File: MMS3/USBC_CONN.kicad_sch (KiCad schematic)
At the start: 7 parts, among them J800 USB_C_Receptacle_USB2.0_16P, U401 TPD2EUSB30DRTR-TP

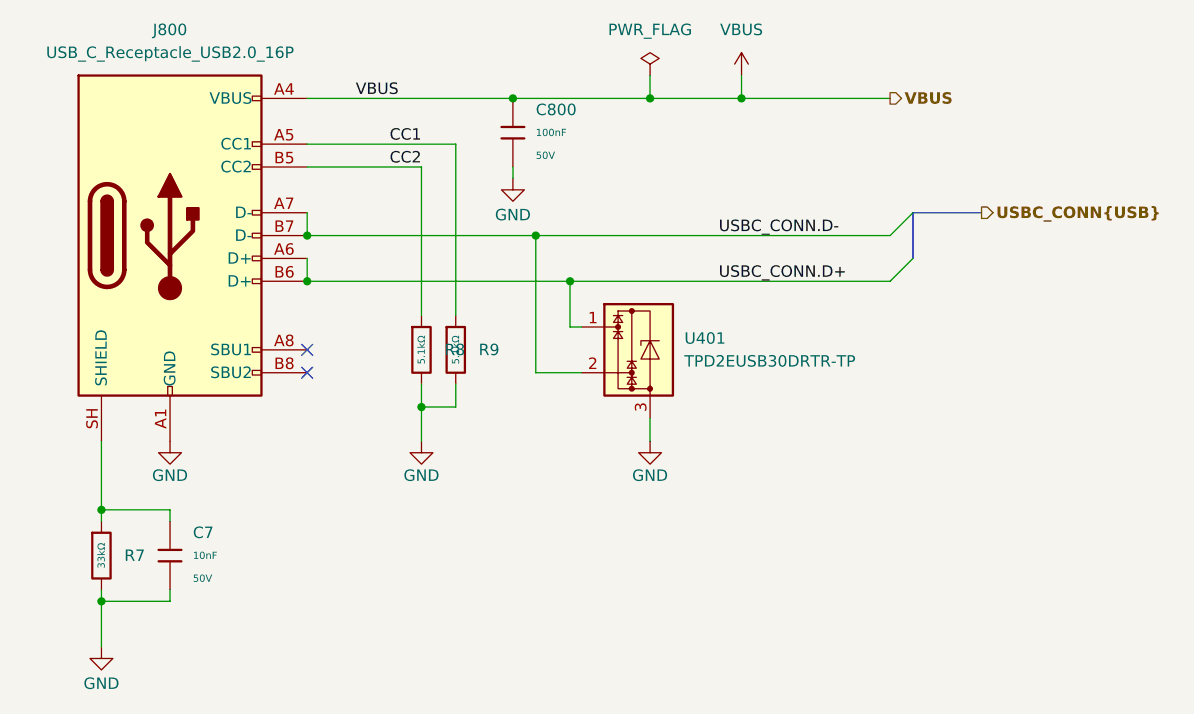
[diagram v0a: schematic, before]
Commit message: changed most of stuff to ch32L103
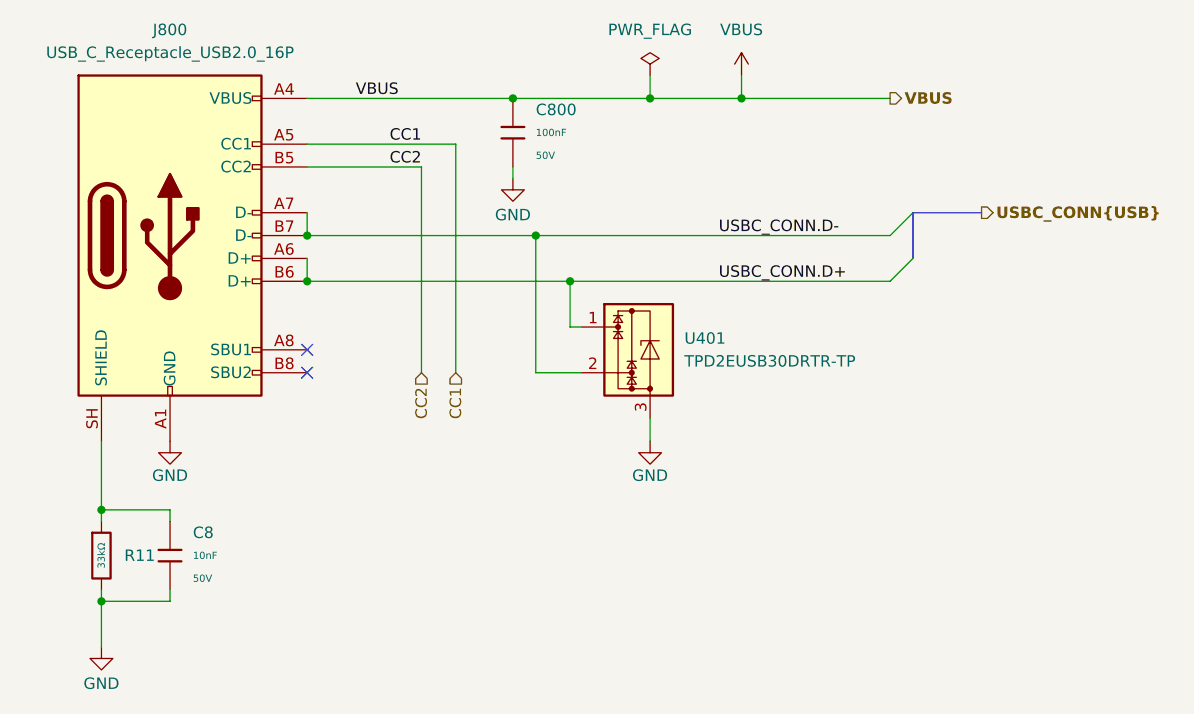
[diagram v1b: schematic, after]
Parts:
- removed R8, R9: 5.1kΩ, PCM_JLCPCB:R_0402, symbol PCM_JLCPCB-Resistors:0402,5.1kΩ
- renumbered C7 to C8, R7 to R11
